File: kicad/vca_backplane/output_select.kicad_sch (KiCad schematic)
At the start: 54 parts, among them J13 AudioJack_729JH, J9 AudioJack_729JH, U10 NE5532, U12 DG442xY, U4 MCP4822, U5 PCA9555PW, U6 DG442xY, U7 AS3360, U9 DG442xY

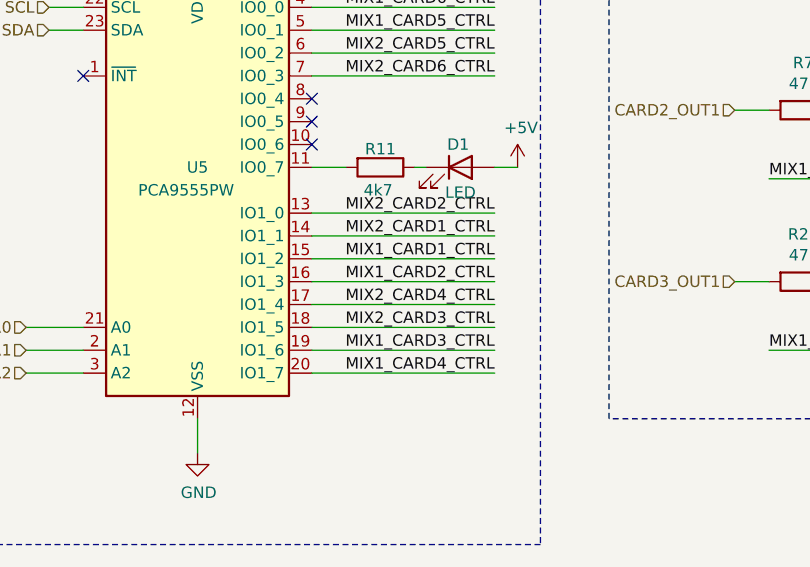
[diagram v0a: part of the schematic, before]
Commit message: add external input sheet.  Basic routing on backplane done- needs cleaning up
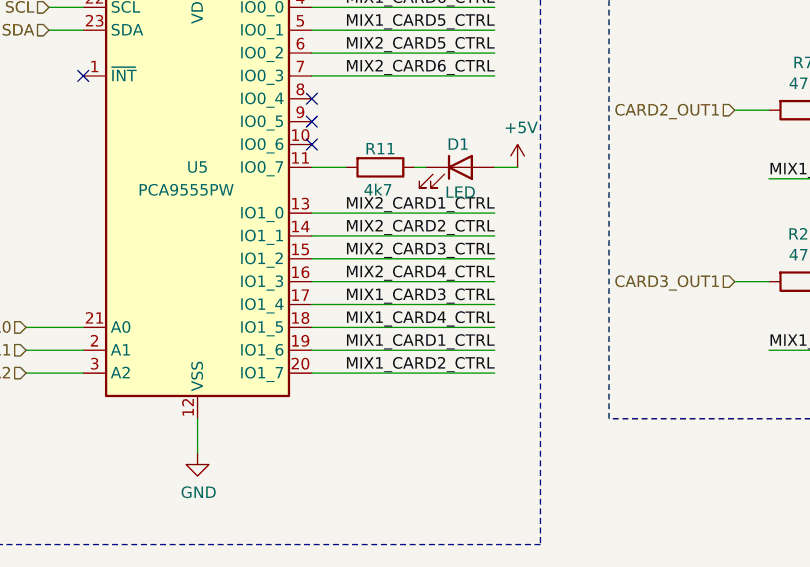
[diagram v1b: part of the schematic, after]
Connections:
- net MIX1_CARD1_CTRL: now also U5.19 (IO1_6); no longer U5.15 (IO1_2)
- net MIX1_CARD2_CTRL: now also U5.20 (IO1_7); no longer U5.16 (IO1_3)
- net MIX1_CARD3_CTRL: now also U5.17 (IO1_4); no longer U5.19 (IO1_6)
- net MIX1_CARD4_CTRL: now also U5.18 (IO1_5); no longer U5.20 (IO1_7)
- net MIX2_CARD1_CTRL: now also U5.13 (IO1_0); no longer U5.14 (IO1_1)
- net MIX2_CARD2_CTRL: now also U5.14 (IO1_1); no longer U5.13 (IO1_0)
- net MIX2_CARD3_CTRL: now also U5.15 (IO1_2); no longer U5.18 (IO1_5)
- net MIX2_CARD4_CTRL: now also U5.16 (IO1_3); no longer U5.17 (IO1_4)
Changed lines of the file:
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@@
     (effects (font (size 1.27 1.27)) (justify left bottom))
   )
-  (label "MIX1_CARD1_CTRL" (at 82.55 69.85 180) (fields_autoplaced)
+  (label "MIX1_CARD1_CTRL" (at 82.55 80.01 180) (fields_autoplaced)
     (effects (font (size 1.27 1.27)) (justify right bottom))
   )
@@
     (effects (font (size 1.27 1.27)) (justify right bottom))
   )
-  (label "MIX1_CARD4_CTRL" (at 82.55 82.55 180) (fields_autoplaced)
+  (label "MIX1_CARD4_CTRL" (at 82.55 77.47 180) (fields_autoplaced)
     (effects (font (size 1.27 1.27)) (justify right bottom))
   )
-  (label "MIX1_CARD3_CTRL" (at 82.55 80.01 180) (fields_autoplaced)
+  (label "MIX1_CARD3_CTRL" (at 82.55 74.93 180) (fields_autoplaced)
     (effects (font (size 1.27 1.27)) (justify right bottom))
   )
@@
     (effects (font (size 1.27 1.27)) (justify right bottom))
   )
-  (label "MIX2_CARD3_CTRL" (at 82.55 77.47 180) (fields_autoplaced)
+  (label "MIX2_CARD3_CTRL" (at 82.55 69.85 180) (fields_autoplaced)
     (effects (font (size 1.27 1.27)) (justify right bottom))
   )
@@
     (effects (font (size 1.27 1.27)) (justify left bottom))
   )
-  (label "MIX2_CARD4_CTRL" (at 82.55 74.93 180) (fields_autoplaced)
+  (label "MIX2_CARD4_CTRL" (at 82.55 72.39 180) (fields_autoplaced)
     (effects (font (size 1.27 1.27)) (justify right bottom))
   )
@@
     (effects (font (size 1.27 1.27)) (justify left bottom))
   )
-  (label "MIX2_CARD1_CTRL" (at 82.55 67.31 180) (fields_autoplaced)
+  (label "MIX2_CARD1_CTRL" (at 82.55 64.77 180) (fields_autoplaced)
     (effects (font (size 1.27 1.27)) (justify right bottom))
   )
@@
     (effects (font (size 1.27 1.27)) (justify right bottom))
   )
-  (label "MIX2_CARD2_CTRL" (at 82.55 64.77 180) (fields_autoplaced)
+  (label "MIX2_CARD2_CTRL" (at 82.55 67.31 180) (fields_autoplaced)
     (effects (font (size 1.27 1.27)) (justify right bottom))
   )
@@
     (effects (font (size 1.27 1.27)) (justify right bottom))
   )
-  (label "MIX1_CARD2_CTRL" (at 82.55 72.39 180) (fields_autoplaced)
+  (label "MIX1_CARD2_CTRL" (at 82.55 82.55 180) (fields_autoplaced)
     (effects (font (size 1.27 1.27)) (justify right bottom))
   )

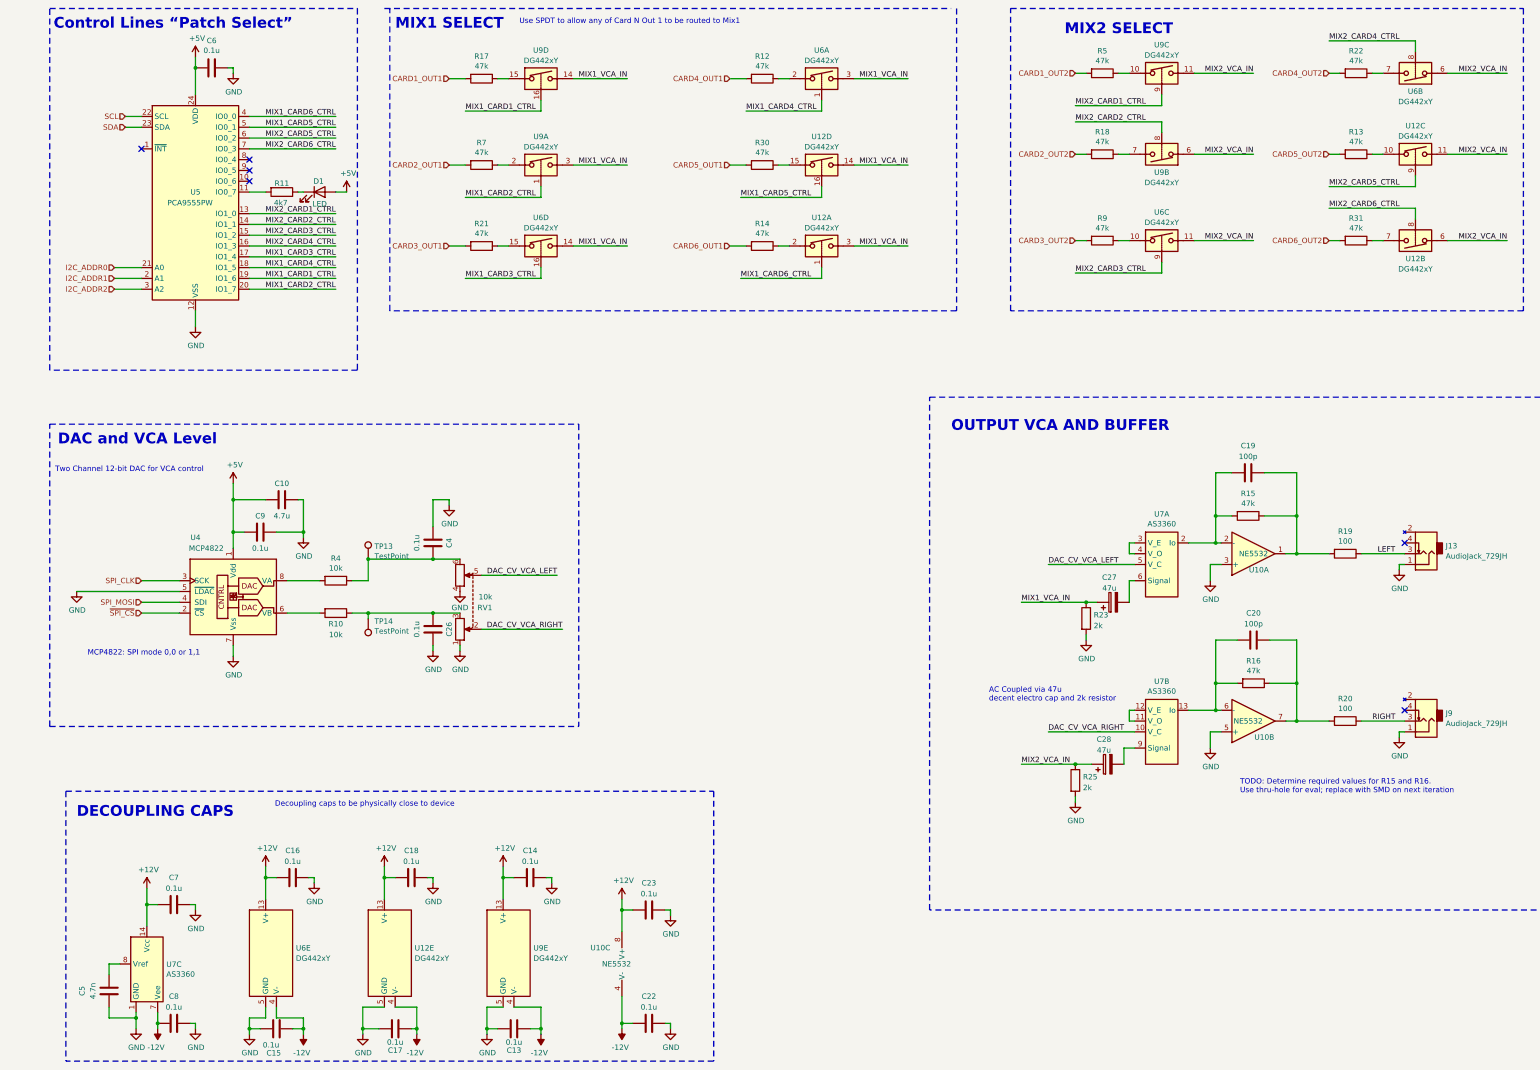
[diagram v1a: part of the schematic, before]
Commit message: geographically reorientated from pcb
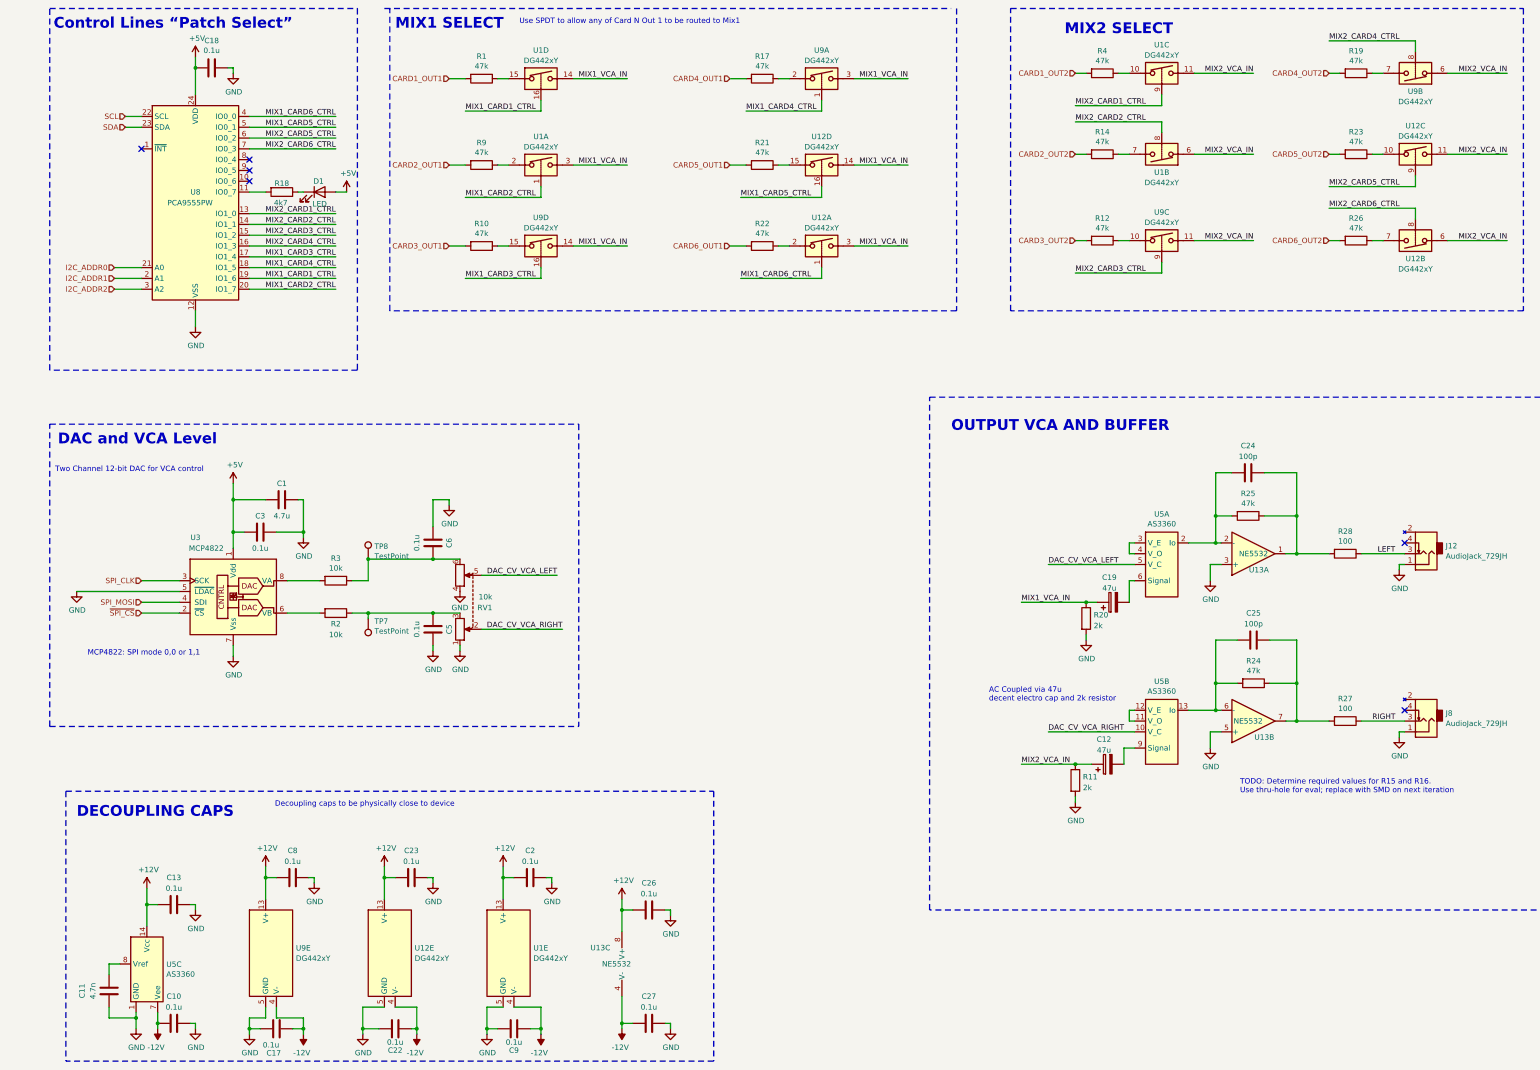
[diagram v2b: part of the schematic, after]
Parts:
- renumbered C10 to C1, C8 to C10, C5 to C11, C28 to C12, C7 to C13, C15 to C17, C6 to C18, C27 to C19, C14 to C2, C17 to C22, C18 to C23, C19 to C24, C20 to C25, C23 to C26, C22 to C27, C9 to C3, C26 to C5, C4 to C6, C16 to C8, C13 to C9, J13 to J12, J9 to J8, R17 to R1, R21 to R10, R25 to R11, R9 to R12, R18 to R14, R12 to R17, R11 to R18, R22 to R19, R10 to R2, R23 to R20, R30 to R21, R14 to R22, R13 to R23, R16 to R24, R15 to R25, R31 to R26, R20 to R27, R19 to R28, R4 to R3, R5 to R4, R7 to R9, TP14 to TP7, TP13 to TP8, U9 to U1, U10 to U13, U4 to U3, U7 to U5, U5 to U8, U6 to U9
